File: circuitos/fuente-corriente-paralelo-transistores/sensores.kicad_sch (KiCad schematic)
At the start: 9 parts, among them U1 LM324

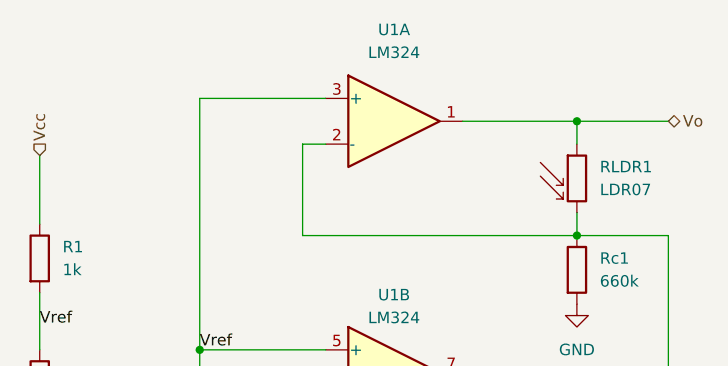
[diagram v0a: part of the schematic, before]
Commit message: pcb con LDRs y led ws2812b-mini
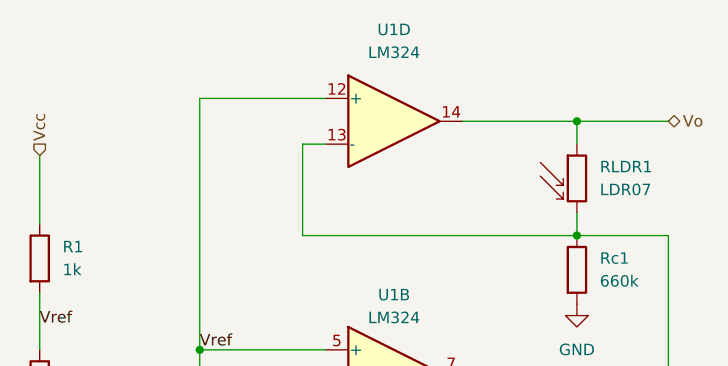
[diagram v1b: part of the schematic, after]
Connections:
- net Vo: now also U1.14; no longer U1.1
- net Vref: now also U1.12 (+); no longer U1.3 (+)
- net at RLDR1.2, RLDR2.2, RLDR3.2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: now also U1.13 (-); no longer U1.2 (-)
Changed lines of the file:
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@@
 		(lib_id "Amplifier_Operational:LM324")
 		(at 114.3 60.96 0)
-		(unit 1)
+		(unit 4)
 		(exclude_from_sim no)
 		(in_bom yes)
@@
 			)
 		)
-		(property "Sim.Library" "/usr/share/kicad/symbols/Simulation_SPICE.sp"
+		(property "Sim.Library" ".\\"
 			(at 114.3 60.96 0)
 			(effects
@@
 			)
 		)
-		(property "Sim.Name" "kicad_builtin_opamp_quad"
-			(at 114.3 60.96 0)
-			(effects
-				(font
-					(size 1.27 1.27)
-				)
-				(hide yes)
-			)
-		)
-		(property "Sim.Device" "SUBCKT"
-			(at 114.3 60.96 0)
-			(effects
-				(font
-					(size 1.27 1.27)
-				)
-				(hide yes)
-			)
-		)
-		(property "Sim.Pins" "1=out1 2=in1- 3=in1+ 4=vcc 5=in2+ 6=in2- 7=out2 8=out3 9=in3- 10=in3+ 11=vee 12=in4+ 13=in4- 14=out4"
-			(at 114.3 60.96 0)
-			(effects
-				(font
-					(size 1.27 1.27)
-				)
-				(hide yes)
-			)
-		)
-		(property "Sim.Params" ""
+		(property "Sim.Name" "<unknown>"
 			(at 114.3 60.96 0)
 			(effects
@@
 				(path "/f36b78d6-8c57-41fd-b61e-747666561b76/55249902-8da7-4028-935b-c0d2fa889b5b"
 					(reference "U1")
-					(unit 1)
+					(unit 4)
 				)
 			)
@@
 			)
 		)
-		(property "Sim.Library" "/usr/share/kicad/symbols/Simulation_SPICE.sp"
+		(property "Sim.Library" ".\\"
 			(at 114.3 88.9 0)
 			(effects
@@
 			)
 		)
-		(property "Sim.Name" "kicad_builtin_opamp_quad"
-			(at 114.3 88.9 0)
-			(effects
-				(font
-					(size 1.27 1.27)
-				)
-				(hide yes)
-			)
-		)
-		(property "Sim.Device" "SUBCKT"
-			(at 114.3 88.9 0)
-			(effects
-				(font
-					(size 1.27 1.27)
-				)
-				(hide yes)
-			)
-		)
-		(property "Sim.Pins" "1=out1 2=in1- 3=in1+ 4=vcc 5=in2+ 6=in2- 7=out2 8=out3 9=in3- 10=in3+ 11=vee 12=in4+ 13=in4- 14=out4"
-			(at 114.3 88.9 0)
-			(effects
-				(font
-					(size 1.27 1.27)
-				)
-				(hide yes)
-			)
-		)
-		(property "Sim.Params" ""
+		(property "Sim.Name" "<unknown>"
 			(at 114.3 88.9 0)
 			(effects
@@
 			)
 		)
-		(property "Sim.Library" "/usr/share/kicad/symbols/Simulation_SPICE.sp"
+		(property "Sim.Library" ".\\"
 			(at 114.3 116.84 0)
 			(effects
@@
 			)
 		)
-		(property "Sim.Name" "kicad_builtin_opamp_quad"
+		(property "Sim.Name" "<unknown>"
 			(at 114.3 116.84 0)
 			(effects
-				(font
-					(size 1.27 1.27)
-				)
-				(hide yes)
-			)
-		)
-		(property "Sim.Device" "SUBCKT"
-			(at 114.3 116.84 0)
-			(effects
-				(font
-					(size 1.27 1.27)
-				)
-				(hide yes)
-			)
-		)
-		(property "Sim.Pins" "1=out1 2=in1- 3=in1+ 4=vcc 5=in2+ 6=in2- 7=out2 8=out3 9=in3- 10=in3+ 11=vee 12=in4+ 13=in4- 14=out4"
-			(at 114.3 116.84 0)
-			(effects
-				(font
-					(size 1.27 1.27)
-				)
-				(hide yes)
-			)
-		)
-		(property "Sim.Params" ""
-			(at 114.3 116.84 0)
-			(effects
